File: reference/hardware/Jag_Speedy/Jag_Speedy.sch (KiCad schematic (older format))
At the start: 1 part, among them U3 Teensy 3.5

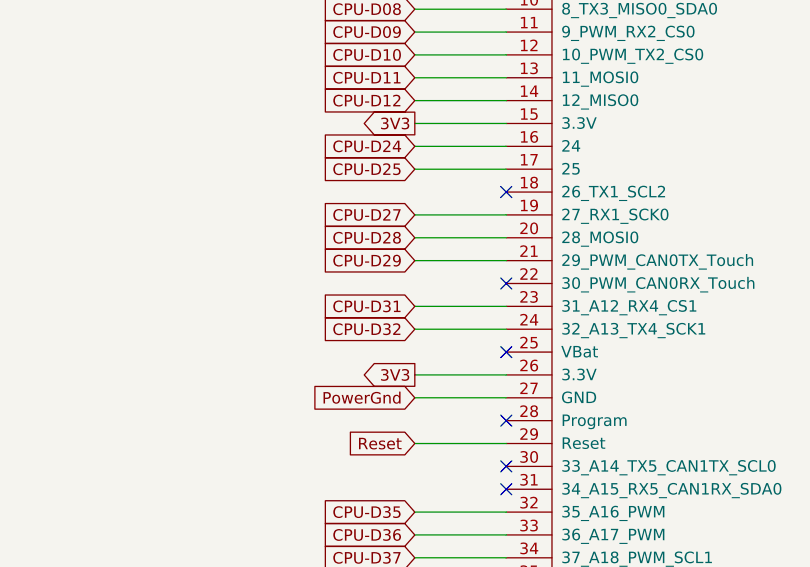
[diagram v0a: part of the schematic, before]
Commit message: Added Water Pump PWM
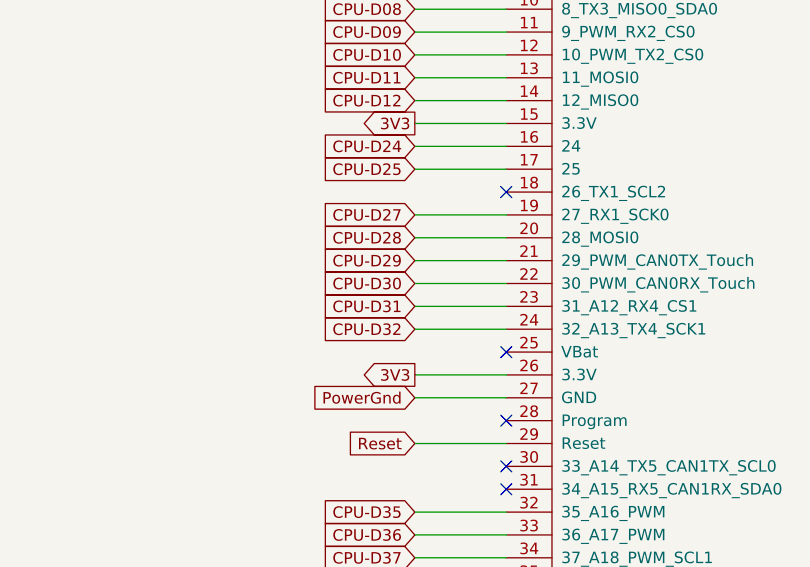
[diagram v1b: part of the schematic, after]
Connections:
- net CPU-D30: now reaches U3.22 (30_PWM_CAN0RX_Touch)
- no-connect marks 40 -> 39
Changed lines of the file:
@@
 	4500 1150 4900 1150
 NoConn ~ 4900 2850
-NoConn ~ 4900 3250
 NoConn ~ 4900 3550
 NoConn ~ 4900 3850
@@
 Wire Wire Line
 	4900 3950 4500 3950
+Text GLabel 4500 3250 0    50   Input ~ 0
+CPU-D30
+Wire Wire Line
+	4900 3250 4500 3250
 $EndSCHEMATC

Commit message: EGR Input
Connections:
- net CPU-A6: now reaches U3.47 (20_A6_PWM_CS0_SCK1)
- no-connect marks 39 -> 38
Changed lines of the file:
@@
 	1    0    0    -1
 $EndComp
-NoConn ~ 7200 5250
 NoConn ~ 4900 4150
 NoConn ~ 4900 4050
@@
 Wire Wire Line
 	4900 3250 4500 3250
+Text GLabel 7500 5250 2    50   Input ~ 0
+CPU-A6
+Wire Wire Line
+	7200 5250 7500 5250
 $EndSCHEMATC
